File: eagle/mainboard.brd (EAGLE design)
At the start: 100 x 100 mm, 73 parts, among them IC1 74HC02D, IC2 74HC151D, IC3 74HC151D, IC4 74HC590D

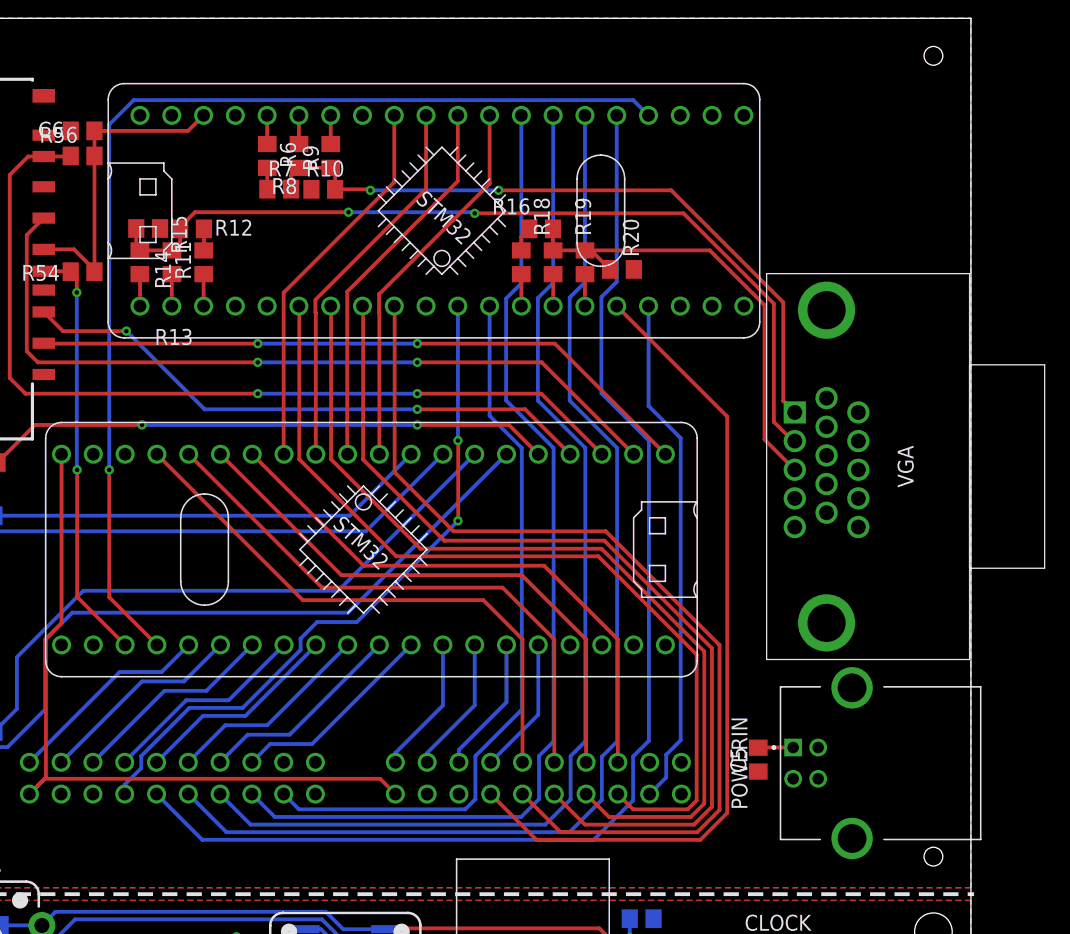
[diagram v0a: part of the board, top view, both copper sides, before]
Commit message: pcb: gpu ready led
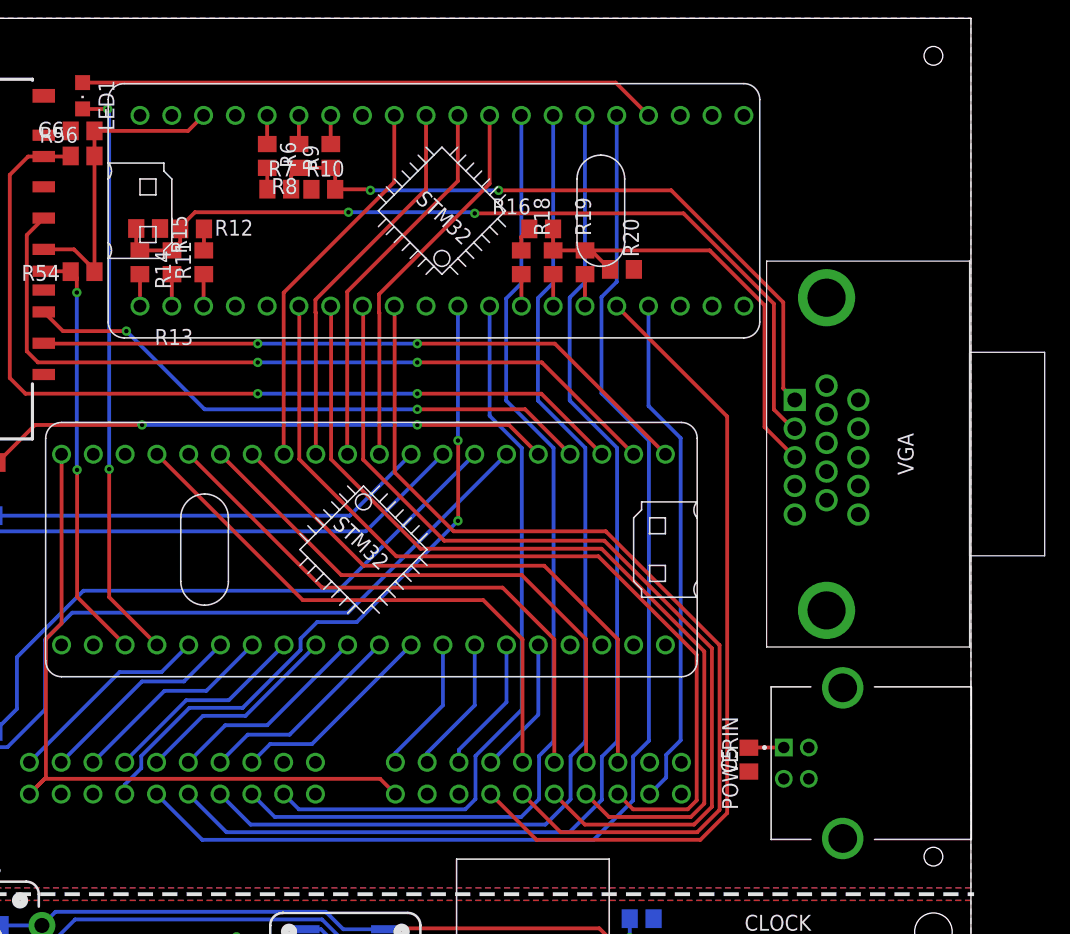
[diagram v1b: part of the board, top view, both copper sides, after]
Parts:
- added LED1: (no value), led:CHIPLED_0805
- moved VGA 1.00 mm to (91.0, 39.5)
- moved C5 0.75 mm to (82.2, 10.8)
- moved POWERIN 0.75 mm to (89.8, 10.5)
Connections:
- new net N$1: GPU.P$37, LED1.A
- net GPU_READY: now also LED1.C; no longer GPU.P$37
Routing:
- net N$1: track 0.00 -> 46.3 mm
- net GPU_READY: track 87.6 -> 46.5 mm, vias 1 -> 2
- net VGA_RED: track 55.1 -> 54.1 mm
- net VGA_GREEN: track 69.3 -> 68.3 mm
- net VGA_BLUE: track 37.2 -> 36.2 mm

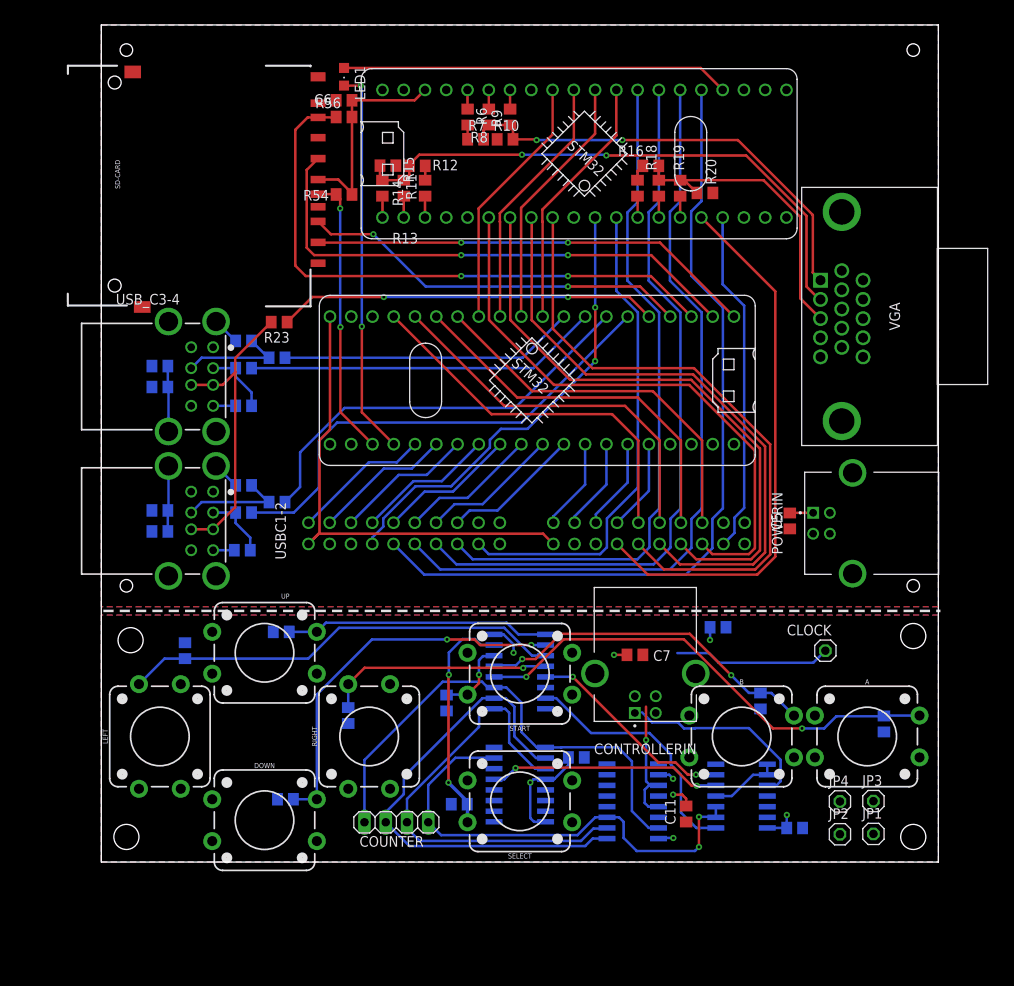
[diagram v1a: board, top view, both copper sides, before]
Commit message: made D-pad quadrtatic, corrected other minor stuff
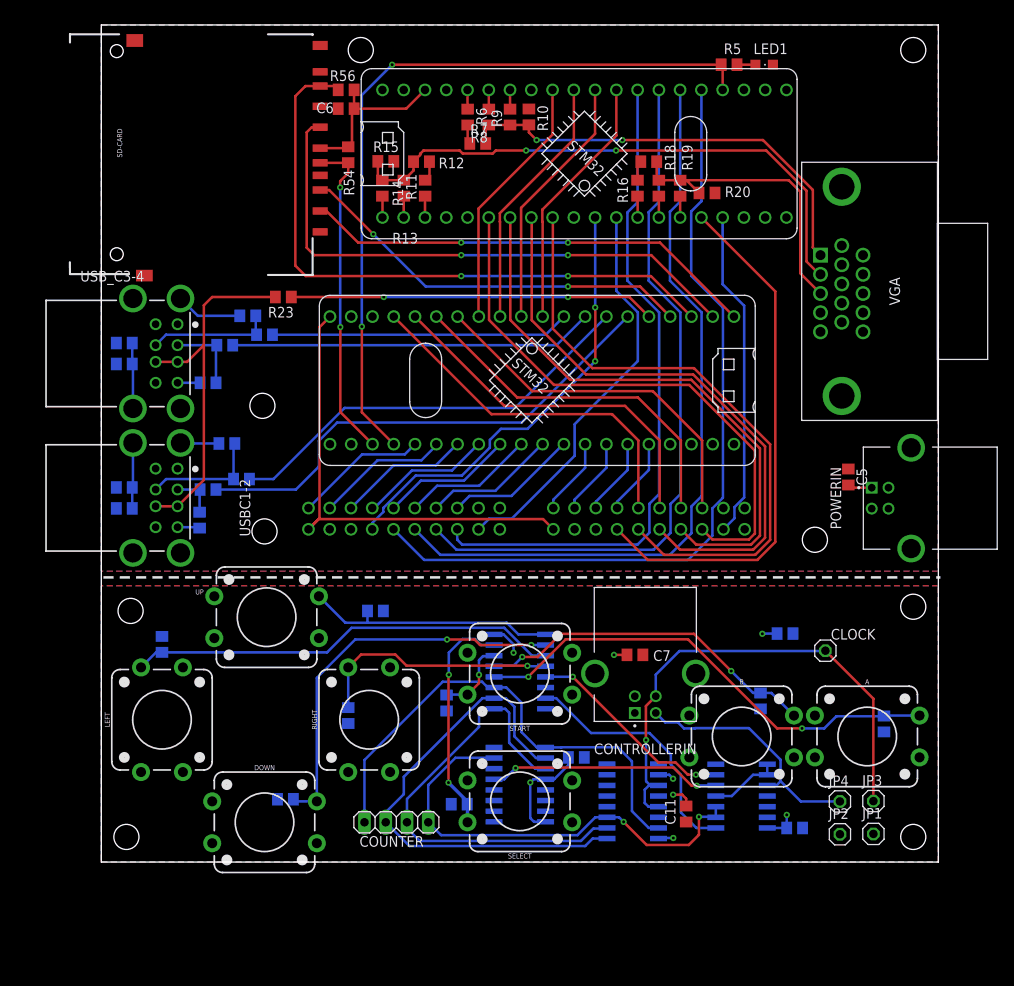
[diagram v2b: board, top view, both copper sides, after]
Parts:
- added R5: 150, rcl:R0805
- moved LED1 50.2 mm to (79.2, 65.2), turned to 270 degrees
- moved R68 11.5 mm to (32.8, 0.00), turned to 180 degrees
- moved C5 8.75 mm to (89.2, 16.0), turned to 90 degrees
- moved C10 8.04 mm to (81.7, -2.71)
- moved POWERIN 7.62 mm to (96.8, 13.5)
- moved R2 6.23 mm to (11.8, 10.8), turned to 90 degrees
- moved R4 5.39 mm to (15.0, 20.0)
- moved C1 5.06 mm to (2.75, 32.0)
- moved C2 5.06 mm to (2.75, 12.2)
- moved C3 5.06 mm to (2.75, 29.5)
- moved C4 5.06 mm to (2.75, 14.8)
- moved R1 5.06 mm to (12.8, 27.2)
- moved R21 5.06 mm to (12.8, 14.5)
- moved R22 5.06 mm to (16.8, 15.8)
- moved USBC1-2 5.06 mm to (2.00, 13.5)
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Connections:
- net GND: now also LED1.C
- net GPU_READY: now also GPU.P$37, R5.1; no longer LED1.C
- net N$1: now also R5.2; no longer GPU.P$37
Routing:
- net GPU_READY: track 46.5 -> 90.9 mm
- net N$1: track 46.3 -> 2.26 mm
- net CONTROLLER_CLOCK: track 34.6 -> 62.0 mm
- net DOUBLE1: track 58.2 -> 47.8 mm
- net C_CLOCK: track 36.1 -> 43.5 mm
- net +3V3: track 84.0 -> 76.6 mm
- net CONTROLLER_OUT: track 23.3 -> 29.7 mm
- net GND: track 27.5 -> 33.6 mm
- net SDHP: track 33.9 -> 39.0 mm
- net SDCLK: track 63.1 -> 67.6 mm
- net SDOUT: track 71.6 -> 75.9 mm
- net N$27: track 57.5 -> 54.9 mm
- net C1_DATA: track 7.91 -> 5.42 mm
- net RIGHT: track 27.3 -> 29.6 mm
- net C4_DATA: track 13.0 -> 14.9 mm
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
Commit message: added svg art and finished todo list
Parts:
- added JP5: (no value), pinhead:1X02
- added LED2: (no value), led:CHIPLED_0805
- added R26: 150, rcl:R0805
- added R27: 10k, rcl:R0805
- moved LED1 8.98 mm to (70.4, 67.2)
- moved R5 7.81 mm to (67.2, 66.2), turned to 90 degrees
- moved VGA 5.50 mm to (91.0, 48.0)
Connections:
- new net N$2: LED2.A, R26.2
- net +5V: now also JP5.1
- net GND: now also R27.2
- net GNDA: now also LED2.C
- net PC14_GPU: now also JP5.2, R27.1
- net VCC: now also R26.1
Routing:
- net PC14_GPU: track 0.00 -> 7.79 mm
- net VGA_RED: track 53.0 -> 47.5 mm
- net VGA_BLUE: track 35.8 -> 30.3 mm
- net VGA_GREEN: track 68.4 -> 63.2 mm
- net N$2: track 0.00 -> 2.00 mm
- net VCC: track 25.8 -> 27.7 mm, vias 6 -> 7

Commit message: pcb: v2 features
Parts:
- added JP6: (no value), pinhead:1X02
- added LED3: (no value), led:CHIPLED_0805
- added R28: 220, rcl:R0805
- added R29: 10k, rcl:R0805
- added S1: TL36PO, switch:TL3XPO
- moved C5 2.51 mm to (89.5, 13.5), turned to 270 degrees
- moved R23 1.75 mm to (23.5, 37.5)
- moved R1 1.59 mm to (14.3, 27.2)
- moved R3 1.59 mm to (19.1, 35.2)
- moved R22 1.50 mm to (18.2, 15.8)
- moved R24 1.50 mm to (16.2, 31.8)
- moved R25 1.50 mm to (21.0, 33.0)
- moved R4 1.35 mm to (16.3, 20.1)
- moved R2 1.25 mm to (13.0, 10.8)
- moved R21 1.25 mm to (14.0, 14.5)
- moved JP5 0.75 mm to (75.5, 66.2)
- moved R27 0.75 mm to (80.8, 66.2)
- moved C1 0.25 mm to (3.00, 32.0), turned to 0 degrees
- moved C2 0.25 mm to (3.00, 12.2), turned to 0 degrees
- moved C3 0.25 mm to (3.00, 29.5), turned to 0 degrees
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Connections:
- removed net N$6: VGA.13
- removed net N$9: VGA.14
- removed net PB15_GPU: GPU.P$4
- new net N$3: POWERIN.1, S1.2
- new net N$4: LED3.A, R28.1
- new net PC14_GPU2: GPU.P$4, JP6.2, R29.1
- net +3V3: now also C1.1, C2.1, C3.1, C4.1, USBC1-2.1, USBC1-2.5, USB_C3-4.1, USB_C3-4.5
- net +5V: now also JP6.1, R28.2, S1.1; no longer C1.1, C2.1, C3.1, C4.1, POWERIN.1, USBC1-2.1, USBC1-2.5, USB_C3-4.1, USB_C3-4.5
- net GND: now also LED3.C, R29.2
- net HSYNC: now also VGA.13
- net VSYNC: now also VGA.14
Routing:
- net VSYNC: track 0.00 -> 62.4 mm, vias 0 -> 1
- net HSYNC: track 0.00 -> 58.6 mm, vias 0 -> 1
- net +3V3: track 76.6 -> 129.8 mm, vias 0 -> 2
- net N$3: track 0.00 -> 9.55 mm
- net +5V: track 2.95 -> 12.1 mm
- net PC14_GPU: track 7.79 -> 0.00 mm
- net GND: track 33.6 -> 40.8 mm
- net PA9_CPU: track 59.5 -> 56.5 mm
- net N$4: track 0.00 -> 2.28 mm
- net VGA_GREEN: track 63.2 -> 61.1 mm
- net VGA_BLUE: track 30.3 -> 28.6 mm
- net PA8_CPU: track 43.7 -> 41.9 mm
- net C_CLOCK: track 43.5 -> 45.2 mm
- net C2_DATA: track 14.1 -> 15.6 mm
- net PA10_CPU1: track 35.7 -> 34.2 mm
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
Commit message: huber approved pcb 2.0
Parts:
- added R30, R31, R32, R33: 10k, rcl:R0805
- S1: value TL36PO -> (none); device switch:TL3XPO -> switches_SparkFun-Switches:SWITCH_SPDT_PTH_11.6X4.0MM
- moved JP6 118.8 mm to (41.2, 67.2)
- moved R29 98.1 mm to (42.2, 49.5)
- moved S1 4.25 mm to (88.2, 22.2), turned to 270 degrees
- moved C5 3.95 mm to (88.2, 17.2)
- moved LED3 3.95 mm to (83.8, 17.5)
- moved R28 3.95 mm to (86.0, 17.2)
- moved VGA 2.26 mm to (91.2, 45.8)
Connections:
- net +5V: now also S1.2; no longer S1.1
- net GND: now also R30.2, R31.2, R32.2, R33.2
- net GPU_MISO: now also R31.1
- net GPU_MOSI: now also R30.1
- net GPU_SCK: now also R32.1
- net GPU_SS: now also R33.1
- net N$3: now also S1.1; no longer S1.2
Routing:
- net PC14_GPU2: track 0.00 -> 20.8 mm, vias 0 -> 1
- net +3V3: track 129.8 -> 143.2 mm, vias 2 -> 1
- net GND: track 40.8 -> 50.1 mm, vias 0 -> 1
- net PC14_GPU: track 0.00 -> 7.04 mm
- net +5V: track 12.1 -> 6.33 mm
- net VGA_GREEN: track 61.1 -> 64.0 mm
- net GPU_MOSI: track 30.8 -> 33.4 mm
- net GPU_MISO: track 30.8 -> 33.3 mm
- net GPU_SS: track 30.8 -> 33.3 mm
- net GPU_SCK: track 30.8 -> 33.3 mm
- net HSYNC: track 58.6 -> 61.0 mm
- net VGA_BLUE: track 28.6 -> 30.9 mm
- net N$3: track 9.55 -> 8.05 mm
- net VGA_RED: track 47.5 -> 48.5 mm
- net VSYNC: track 62.4 -> 63.2 mm
